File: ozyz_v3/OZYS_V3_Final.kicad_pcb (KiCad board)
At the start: 4 copper layers, 56 x 69 mm, 113 parts, among them CN1 532610571, J2 Conn_01x02_Pin, J3 AudioJack4, J4 AudioJack4, J5 AudioJack4, J6 AudioJack4, Q1 AO3400A, Q2 AO3401A, U1 ISO1044BD, U10 FTC252012S1R5MBCA (1.5uF 2.9A)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

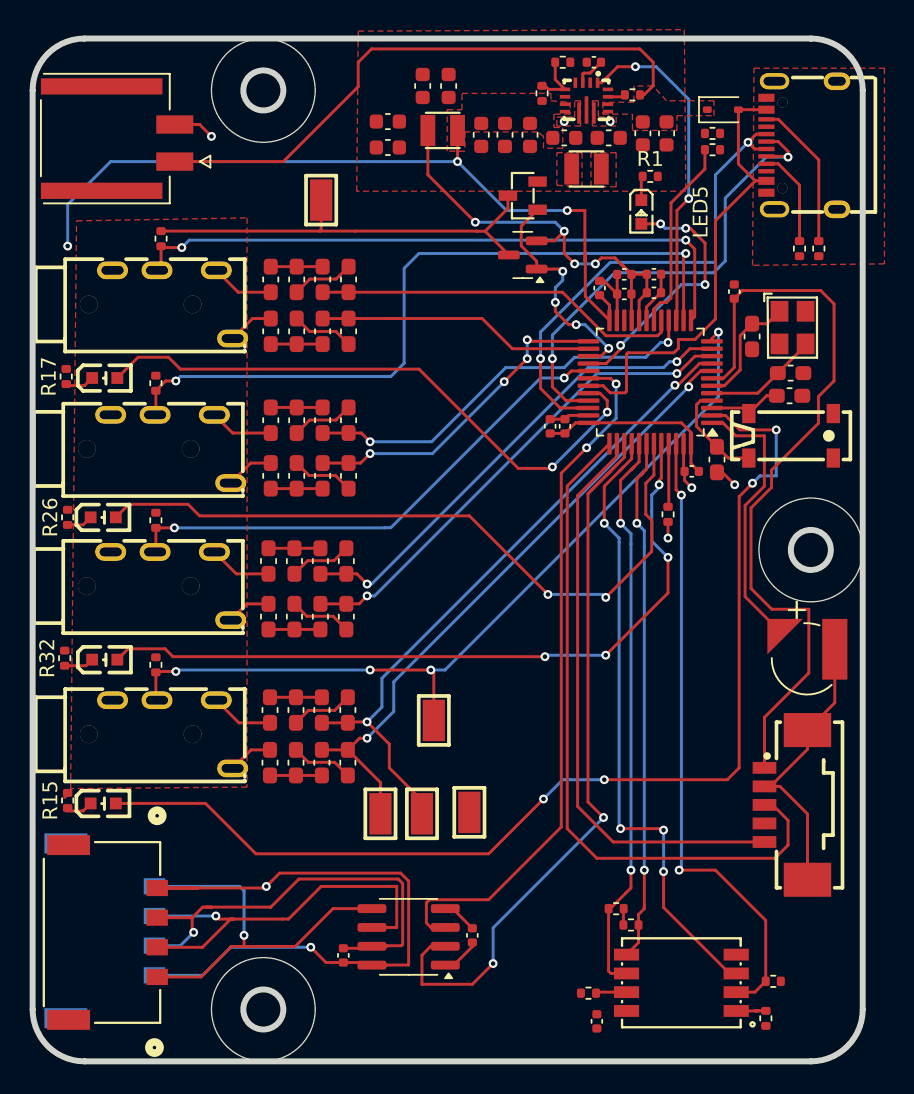
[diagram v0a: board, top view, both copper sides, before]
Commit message: Updated with Pours
Only missing gnd pours on top and bottom copper planes
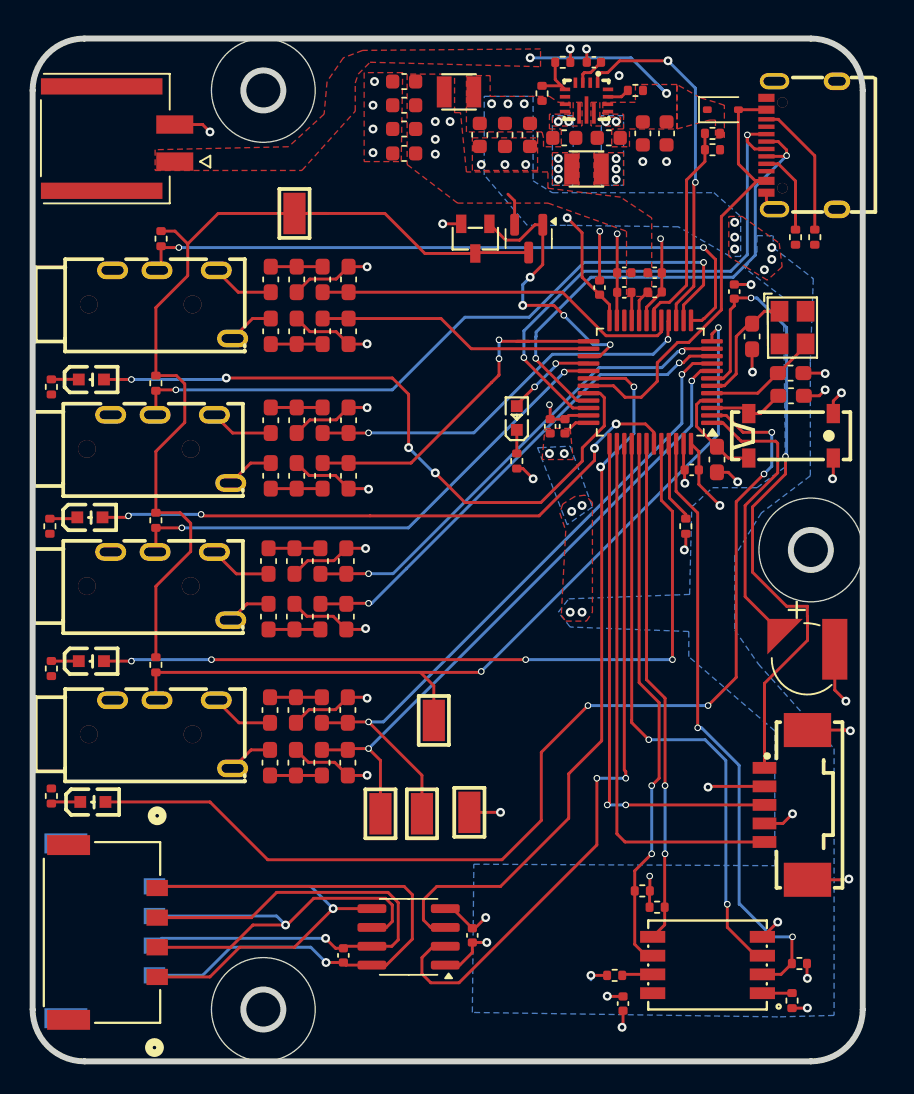
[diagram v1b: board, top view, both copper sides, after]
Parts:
- moved R1 21.2 mm to (52.6, 47.0), turned to -90 degrees
- moved LED5 16.2 mm to (52.6, 44.1), turned to 90 degrees
- moved Q1 4.32 mm to (49.8, 32.0), turned to 90 degrees
- moved C44 3.01 mm to (45.0, 21.4), turned to 0 degrees
- moved U10 2.82 mm to (48.7, 22.1)
- moved C13 2.13 mm to (59.8, 83.6)
- moved R2 2.13 mm to (61.1, 76.0)
- moved R3 2.13 mm to (62.1, 77.1)
- moved R38 2.13 mm to (59.2, 81.7)
- moved U3 2.13 mm to (65.5, 81.0)
- moved R4 2.13 mm to (71.2, 83.4)
- moved R5 2.13 mm to (71.7, 80.9)
- moved U8 2.01 mm to (37.6, 30.3), turned to -90 degrees
- moved C43 1.80 mm to (45.0, 23.0), turned to 0 degrees
- moved R37 1.44 mm to (64.0, 51.4)
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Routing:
- net +3V3: track 69.7 -> 27.8 mm, vias 3 -> 24
- net 3V3A_SW: track 29.3 -> 63.5 mm
- net GND: track 75.3 -> 107.8 mm, vias 5 -> 44
- net Net-(D2-K): track 39.5 -> 11.0 mm, vias 0 -> 2
- net +3V3A: track 31.3 -> 6.30 mm
- net /SWDIO: track 46.9 -> 35.0 mm, vias 0 -> 2
- net /STATUS_LED: track 17.9 -> 6.20 mm, vias 4 -> 2
- net /nRST: track 51.7 -> 45.0 mm, vias 0 -> 2
- net /LED3: track 48.1 -> 41.5 mm, vias 2 -> 4
- net Net-(J_CAN1-Pin_2): track 30.4 -> 36.9 mm
- net /LED2: track 40.6 -> 45.1 mm, vias 2 -> 4
- net Net-(J_CAN1-Pin_1): track 44.5 -> 39.9 mm, vias 2 -> 1
- net /CAN_TXD: track 51.8 -> 47.9 mm
- net /3V3A_SW_EN: track 15.8 -> 19.3 mm
- net /LED4: track 50.2 -> 53.3 mm
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- added copper zone on B.Cu, net +3V3
- added copper zone on F.Cu, net +3V3A
- added copper zone on B.Cu, net Net-(U4-L1)
- added copper zone on B.Cu, net Net-(U4-L2)
- removed copper zone on F.Cu, net 3V3A_SW
